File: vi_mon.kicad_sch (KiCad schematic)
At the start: 20 parts, among them U15 LTC2991CMS_TRPBF, U16 LTC2991CMS_TRPBF, U18 LTC2991CMS_TRPBF

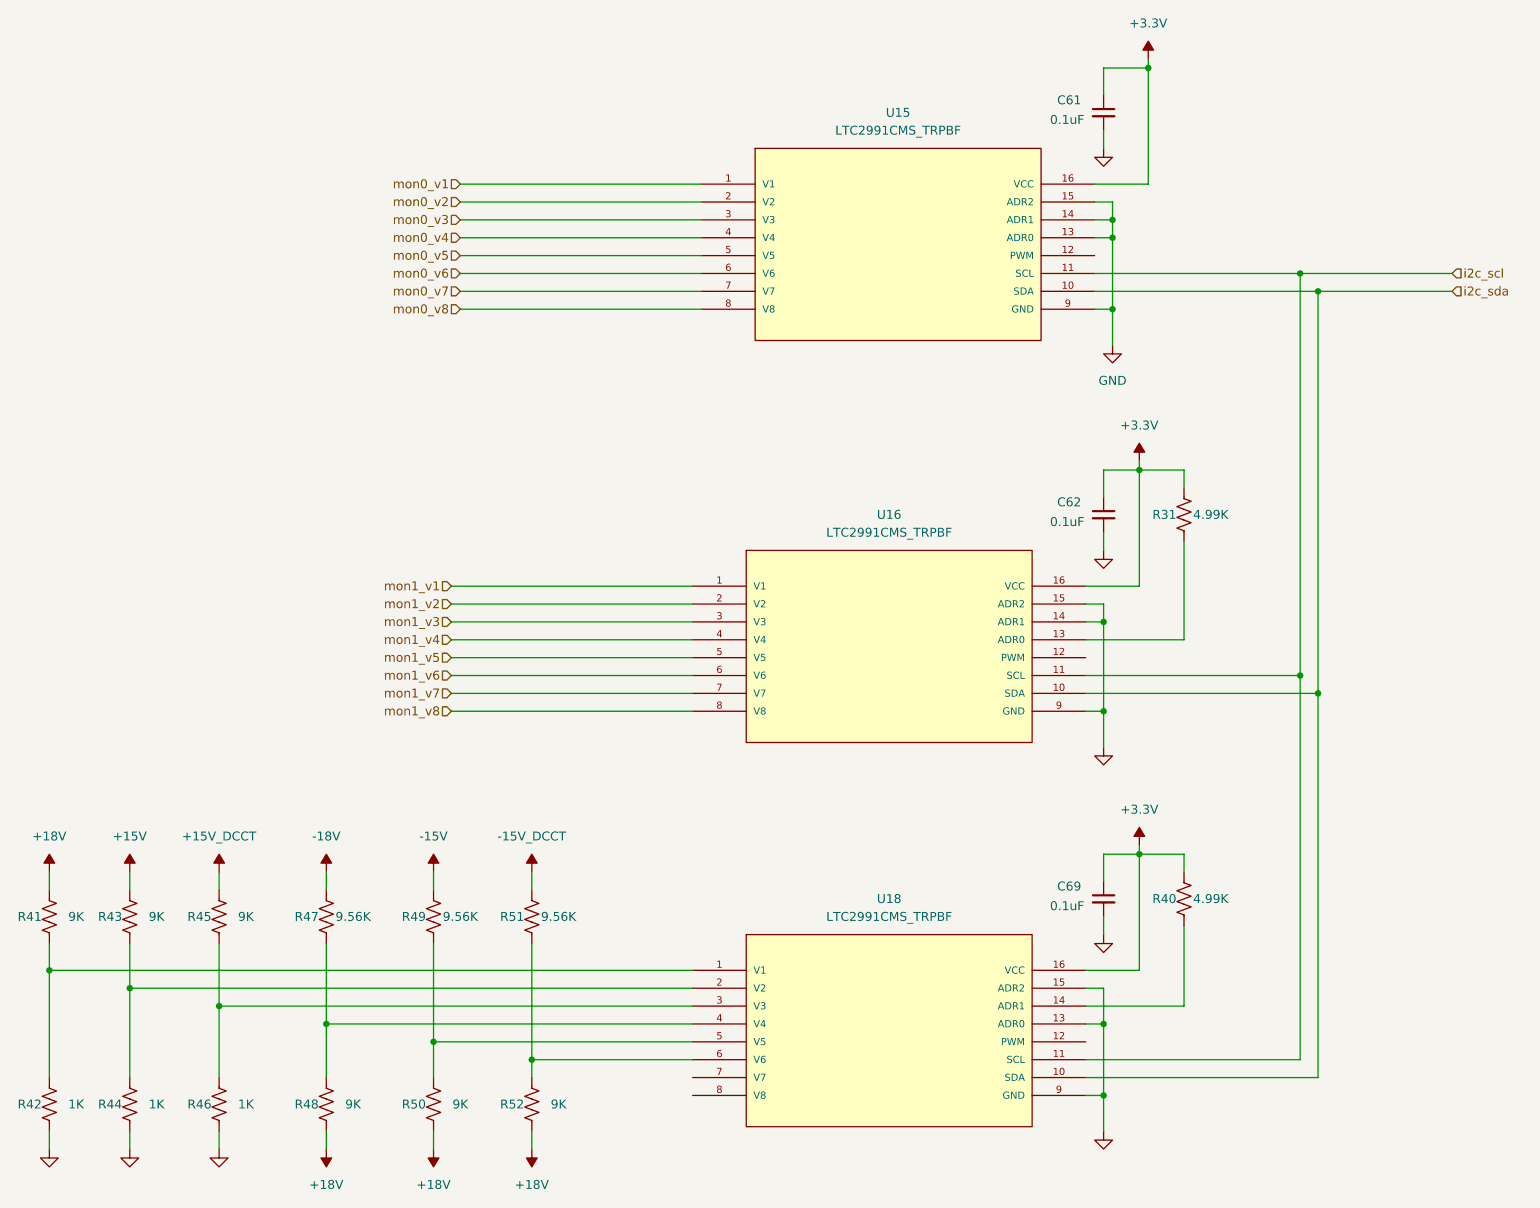
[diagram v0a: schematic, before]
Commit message: Add all 4 channels
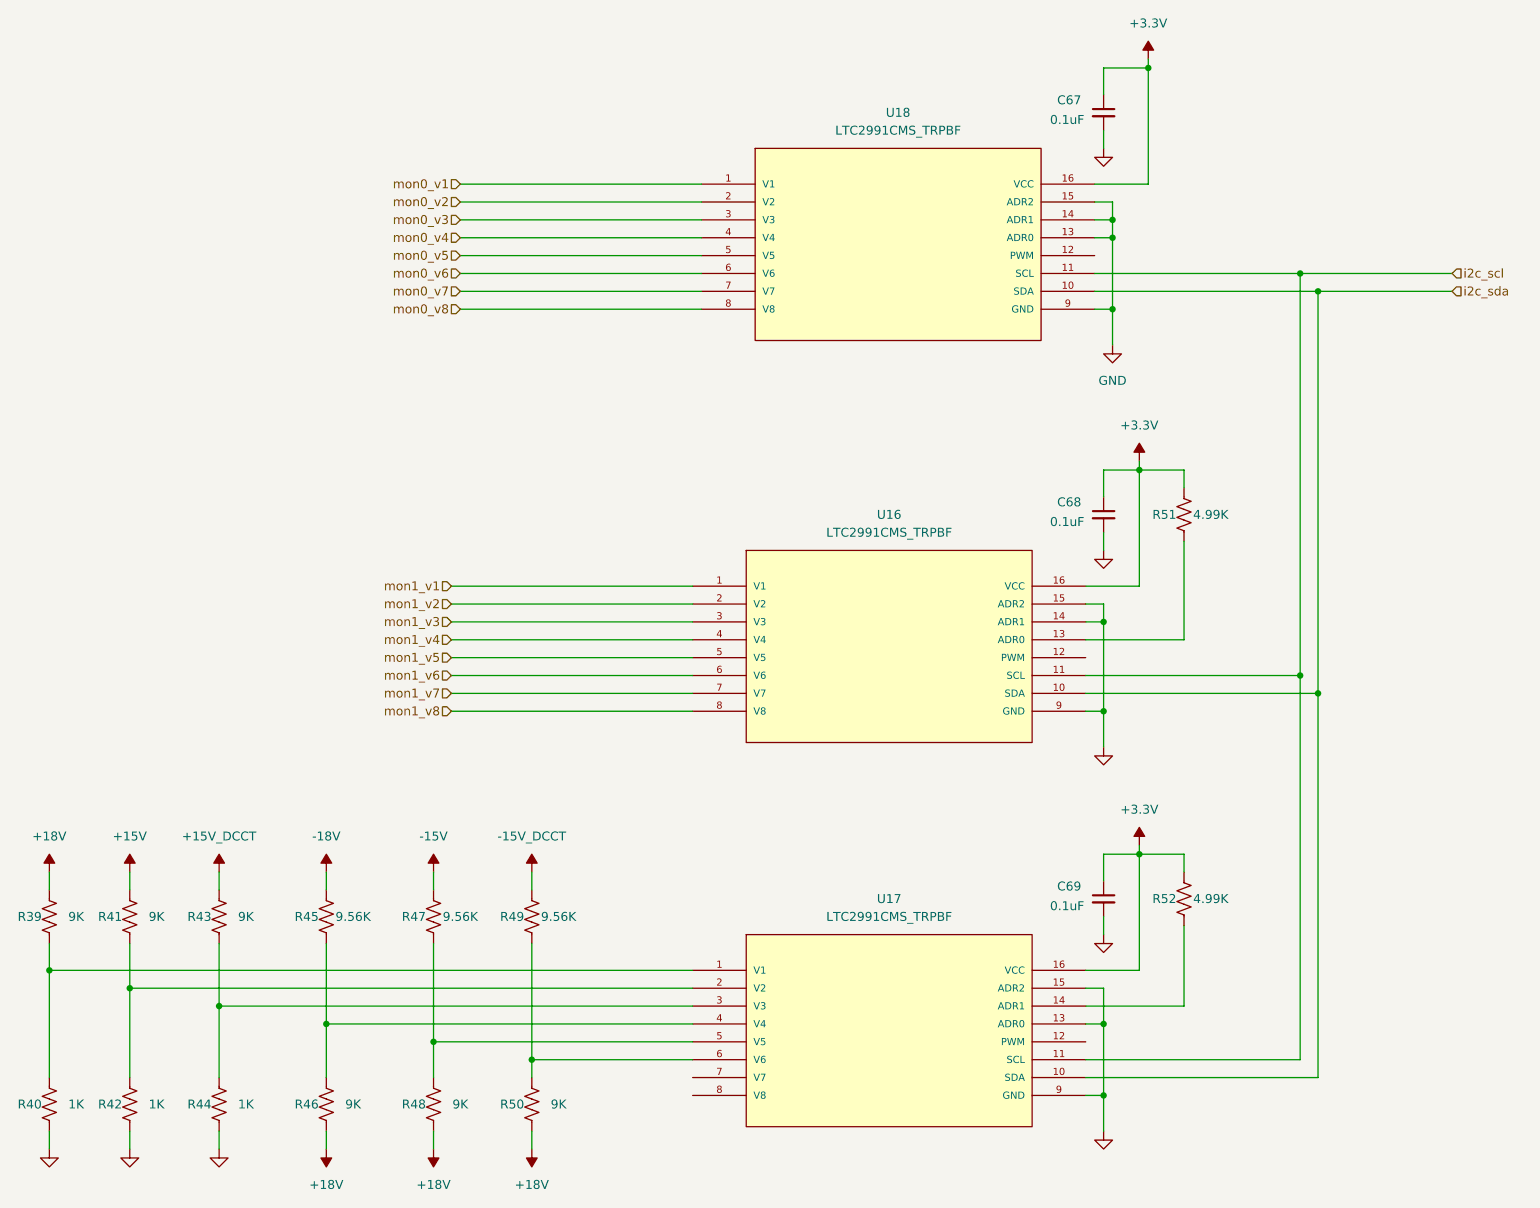
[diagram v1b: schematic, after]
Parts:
- renumbered C61 to C67, C62 to C68, R41 to R39, R42 to R40, R43 to R41, R44 to R42, R45 to R43, R46 to R44, R47 to R45, R48 to R46, R49 to R47, R50 to R48, R51 to R49, R52 to R50, R31 to R51, R40 to R52, U18 to U17, U15 to U18

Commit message: Start routing
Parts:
- renumbered C67 to C57, C68 to C58, C69 to C59, R39 to R36, R40 to R37, R41 to R38, R42 to R39, R43 to R40, R44 to R41, R45 to R42, R46 to R43, R47 to R44, R48 to R45, R49 to R46, R50 to R47, R51 to R48, R52 to R49, U16 to U12, U17 to U13, U18 to U14
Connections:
- net mon1_v1: no longer names the net of U12.1 (V1)
- net mon1_v2: no longer names the net of U12.2 (V2)
- no-connect marks 0 -> 6

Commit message: Finished layout
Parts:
- C57, C58, C59: Cost (none) -> .01; MFG (none) -> Taiyo Yuden; MFG_PN (none) -> TMK105BJ104KV-F
- R36, R38, R40, R43, R45, R47: value 9K -> 9.09K; Cost (none) -> 0.01; MFG (none) -> Panasonic; MFG_PN (none) -> ERJ-2RKF9091X
- R37, R39, R41: value 1K -> 1.0K; Cost (none) -> 0.01; MFG (none) -> Panasonic; MFG_PN (none) -> ERJ-2RKF1001X
- R42, R44, R46: value 9.56K -> 9.53K; Cost (none) -> 0.01; MFG (none) -> Panasonic; MFG_PN (none) -> ERJ-2RKF9531X
- R48, R49: Cost (none) -> 0.01; MFG (none) -> Panasonic; MFG_PN (none) -> ERJ-2RKF4991X
- U12, U13, U14: MFG (none) -> Analog Devices; MFG_PN (none) -> LTC2991CMS#TRPBF
